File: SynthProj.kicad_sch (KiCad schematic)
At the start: 29 parts, among them J18 Ext In

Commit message: routing work...
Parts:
- added SW5: SW_DPDT_x2, SynthProjConnectors:MTS-203-A1-T0, symbol Switch:SW_DPDT_x2
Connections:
- net PT2399Echo/EchoOut: now also SW5.5 (B); no longer J?.T
- net PT2399Echo/Echo_ExtIn: now also SW5.2 (B); no longer J?.T
- new net: J?.T, SW5.1 (A)
- new net: J?.T, SW5.4 (A)
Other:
- moved on the sheet: J?
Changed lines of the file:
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@@
     (stroke (width 0) (type default))
   )
-  (wire (pts (xy 305.435 88.265) (xy 311.785 88.265))
+  (wire (pts (xy 292.735 88.265) (xy 299.085 88.265))
     (stroke (width 0) (type default))
   )
@@
     (stroke (width 0) (type default))
   )
+  (wire (pts (xy 368.3 73.025) (xy 380.365 73.025))
+    (stroke (width 0) (type default))
+  )
   (wire (pts (xy 118.11 64.135) (xy 134.62 64.135))
     (stroke (width 0) (type default))
@@
     (stroke (width 0) (type default))
   )
+  (wire (pts (xy 309.245 90.805) (xy 311.785 90.805))
+    (stroke (width 0) (type default))
+  )
   (wire (pts (xy 368.935 149.86) (xy 368.935 145.415))
     (stroke (width 0) (type default))
@@
     (stroke (width 0) (type default))
   )
-  (wire (pts (xy 311.785 88.265) (xy 311.785 77.47))
+  (wire (pts (xy 311.785 77.47) (xy 311.785 90.805))
     (stroke (width 0) (type default))
   )
@@
     (stroke (width 0) (type default))
   )
+  (wire (pts (xy 299.085 93.345) (xy 296.545 93.345))
+    (stroke (width 0) (type default))
+  )
   (wire (pts (xy 115.57 62.865) (xy 115.57 66.675))
     (stroke (width 0) (type default))
@@
     (stroke (width 0) (type default))
   )
+  (wire (pts (xy 285.75 101.6) (xy 296.545 101.6))
+    (stroke (width 0) (type default))
+  )
   (wire (pts (xy 127 118.745) (xy 127 74.295))
     (stroke (width 0) (type default))
   )
+  (wire (pts (xy 296.545 93.345) (xy 296.545 101.6))
+    (stroke (width 0) (type default))
+  )
   (wire (pts (xy 305.435 75.565) (xy 318.77 75.565))
     (stroke (width 0) (type default))
@@
     (stroke (width 0) (type default))
   )
-  (wire (pts (xy 354.965 75.565) (xy 361.315 75.565))
+  (wire (pts (xy 354.965 75.565) (xy 358.14 75.565))
     (stroke (width 0) (type default))
   )
@@
   )
   (wire (pts (xy 306.07 152.4) (xy 318.135 152.4))
+    (stroke (width 0) (type default))
+  )
+  (wire (pts (xy 382.905 78.105) (xy 368.3 78.105))
     (stroke (width 0) (type default))
   )
@@
     )
   )
-  (symbol (lib_id "power:GNDREF") (at 361.315 73.025 0) (unit 1)
+  (symbol (lib_id "power:GNDREF") (at 382.905 75.565 0) (unit 1)
     (in_bom yes) (on_board yes) (dnp no) (fields_autoplaced)
-    (property "Reference" "#PWR034" (at 361.315 79.375 0)
-      (effects (font (size 1.27 1.27)) hide)
-    )
-    (property "Value" "GNDREF" (at 361.315 77.1581 0)
-      (effects (font (size 1.27 1.27)))
-    )
-    (property "Footprint" "" (at 361.315 73.025 0)
-      (effects (font (size 1.27 1.27)) hide)
-    )
-    (property "Datasheet" "" (at 361.315 73.025 0)
+    (property "Reference" "#PWR034" (at 382.905 81.915 0)
+      (effects (font (size 1.27 1.27)) hide)
+    )
+    (property "Value" "GNDREF" (at 382.905 79.6981 0)
+      (effects (font (size 1.27 1.27)))
+    )
+    (property "Footprint" "" (at 382.905 75.565 0)
+      (effects (font (size 1.27 1.27)) hide)
+    )
+    (property "Datasheet" "" (at 382.905 75.565 0)
       (effects (font (size 1.27 1.27)) hide)
     )
@@
     )
   )
-  (symbol (lib_id "SynthProj-rescue:AudioJack2-Connector") (at 300.355 88.265 0) (unit 1)
-    (in_bom yes) (on_board yes) (dnp no)
-    (property "Reference" "J?" (at 301.1678 80.01 0)
-      (effects (font (size 1.27 1.27)))
-    )
-    (property "Value" "Echo_ExtIn" (at 301.1678 82.3214 0)
-      (effects (font (size 1.27 1.27)))
-    )
-    (property "Footprint" "SynthProjConnectors:PJ-301" (at 300.355 88.265 0)
-      (effects (font (size 1.27 1.27)) hide)
-    )
-    (property "Datasheet" "~" (at 300.355 88.265 0)
+  (symbol (lib_id "SynthProj-rescue:AudioJack2-Connector") (at 287.655 88.265 0) (unit 1)
+    (in_bom yes) (on_board yes) (dnp no)
+    (property "Reference" "J?" (at 288.4678 80.01 0)
+      (effects (font (size 1.27 1.27)))
+    )
+    (property "Value" "Echo_ExtIn" (at 288.4678 82.3214 0)
+      (effects (font (size 1.27 1.27)))
+    )
+    (property "Footprint" "SynthProjConnectors:PJ-301" (at 287.655 88.265 0)
+      (effects (font (size 1.27 1.27)) hide)
+    )
+    (property "Datasheet" "~" (at 287.655 88.265 0)
       (effects (font (size 1.27 1.27)) hide)
     )
@@
     )
   )
-  (symbol (lib_id "SynthProj-rescue:AudioJack2-Connector") (at 366.395 75.565 0) (mirror y) (unit 1)
-    (in_bom yes) (on_board yes) (dnp no)
-    (property "Reference" "J?" (at 365.5822 67.31 0)
-      (effects (font (size 1.27 1.27)))
-    )
-    (property "Value" "ECHO_OUT" (at 365.5822 69.6214 0)
-      (effects (font (size 1.27 1.27)))
-    )
-    (property "Footprint" "SynthProjConnectors:PJ-301" (at 366.395 75.565 0)
-      (effects (font (size 1.27 1.27)) hide)
-    )
-    (property "Datasheet" "~" (at 366.395 75.565 0)
+  (symbol (lib_id "SynthProj-rescue:AudioJack2-Connector") (at 387.985 78.105 0) (mirror y) (unit 1)
+    (in_bom yes) (on_board yes) (dnp no)
+    (property "Reference" "J?" (at 387.1722 69.85 0)
+      (effects (font (size 1.27 1.27)))
+    )
+    (property "Value" "ECHO_OUT" (at 387.1722 72.1614 0)
+      (effects (font (size 1.27 1.27)))
+    )
+    (property "Footprint" "SynthProjConnectors:PJ-301" (at 387.985 78.105 0)
+      (effects (font (size 1.27 1.27)) hide)
+    )
+    (property "Datasheet" "~" (at 387.985 78.105 0)
       (effects (font (size 1.27 1.27)) hide)
     )
@@
     )
   )
+  (symbol (lib_id "Switch:SW_DPDT_x2") (at 304.165 90.805 0) (mirror y) (unit 1)
+    (in_bom yes) (on_board yes) (dnp no)
+    (property "Reference" "SW5" (at 304.165 86.995 0)
+      (effects (font (size 1.27 1.27)))
+    )
+    (property "Value" "SW_DPDT_x2" (at 304.165 84.5708 0)
+      (effects (font (size 1.27 1.27)))
+    )
+    (property "Footprint" "SynthProjConnectors:MTS-203-A1-T0" (at 304.165 90.805 0)
+      (effects (font (size 1.27 1.27)) hide)
+    )
+    (property "Datasheet" "~" (at 304.165 90.805 0)
+      (effects (font (size 1.27 1.27)) hide)
+    )
+    (pin "2")
+    (pin "5")
+    (pin "3")
+    (pin "6")
+    (pin "4")
+    (pin "1")
+    (instances
+      (project "SynthProj"
+        (path "/9021c97e-351f-4ed9-b393-50257df6a463/0e948a88-c071-4754-aa3e-af223f738530"
+          (reference "SW5") (unit 1)
+        )
+        (path "/9021c97e-351f-4ed9-b393-50257df6a463"
+          (reference "SW5") (unit 1)
+        )
+      )
+    )
+  )
   (symbol (lib_id "power:GNDREF") (at 153.67 139.7 0) (unit 1)
     (in_bom yes) (on_board yes) (dnp no) (fields_autoplaced)
@@
     )
   )
+  (symbol (lib_id "Switch:SW_DPDT_x2") (at 363.22 75.565 0) (mirror x) (unit 2)
+    (in_bom yes) (on_board yes) (dnp no)
+    (property "Reference" "SW5" (at 363.22 68.4997 0)
+      (effects (font (size 1.27 1.27)))
+    )
+    (property "Value" "SW_DPDT_x2" (at 363.22 70.9239 0)
+      (effects (font (size 1.27 1.27)))
+    )
+    (property "Footprint" "SynthProjConnectors:MTS-203-A1-T0" (at 363.22 75.565 0)
+      (effects (font (size 1.27 1.27)) hide)
+    )
+    (property "Datasheet" "~" (at 363.22 75.565 0)
+      (effects (font (size 1.27 1.27)) hide)
+    )
+    (pin "2")
+    (pin "5")
+    (pin "3")
+    (pin "6")
+    (pin "4")
+    (pin "1")
+    (instances
+      (project "SynthProj"
+        (path "/9021c97e-351f-4ed9-b393-50257df6a463/0e948a88-c071-4754-aa3e-af223f738530"
+          (reference "SW5") (unit 2)
+        )
+        (path "/9021c97e-351f-4ed9-b393-50257df6a463"
+          (reference "SW5") (unit 2)
+        )
+      )
+    )
+  )
   (symbol (lib_id "SynthProj-rescue:AudioJack2-Connector") (at 64.77 34.925 0) (unit 1)
     (in_bom yes) (on_board yes) (dnp no)
@@
     )
   )
-  (symbol (lib_id "power:GNDREF") (at 305.435 85.725 0) (unit 1)
+  (symbol (lib_id "power:GNDREF") (at 292.735 85.725 0) (unit 1)
     (in_bom yes) (on_board yes) (dnp no) (fields_autoplaced)
-    (property "Reference" "#PWR033" (at 305.435 92.075 0)
-      (effects (font (size 1.27 1.27)) hide)
-    )
-    (property "Value" "GNDREF" (at 305.435 89.8581 0)
-      (effects (font (size 1.27 1.27)))
-    )
-    (property "Footprint" "" (at 305.435 85.725 0)
-      (effects (font (size 1.27 1.27)) hide)
-    )
-    (property "Datasheet" "" (at 305.435 85.725 0)
-      (effects (font (size 1.27 1.27)) hide)
-    )
+    (property "Reference" "#PWR033" (at 292.735 92.075 0)
+      (effects (font (size 1.27 1.27)) hide)
+    )
+    (property "Value" "GNDREF" (at 292.735 89.8581 0)
+      (effects (font (size 1.27 1.27)))
+    )
+    (property "Footprint" "" (at 292.735 85.725 0)
+      (effects (font (size 1.27 1.27)) hide)
+    )
+    (property "Datasheet" "" (at 292.735 85.725 0)
+      (effects (font (size 1.27 1.27)) hide)
+    )

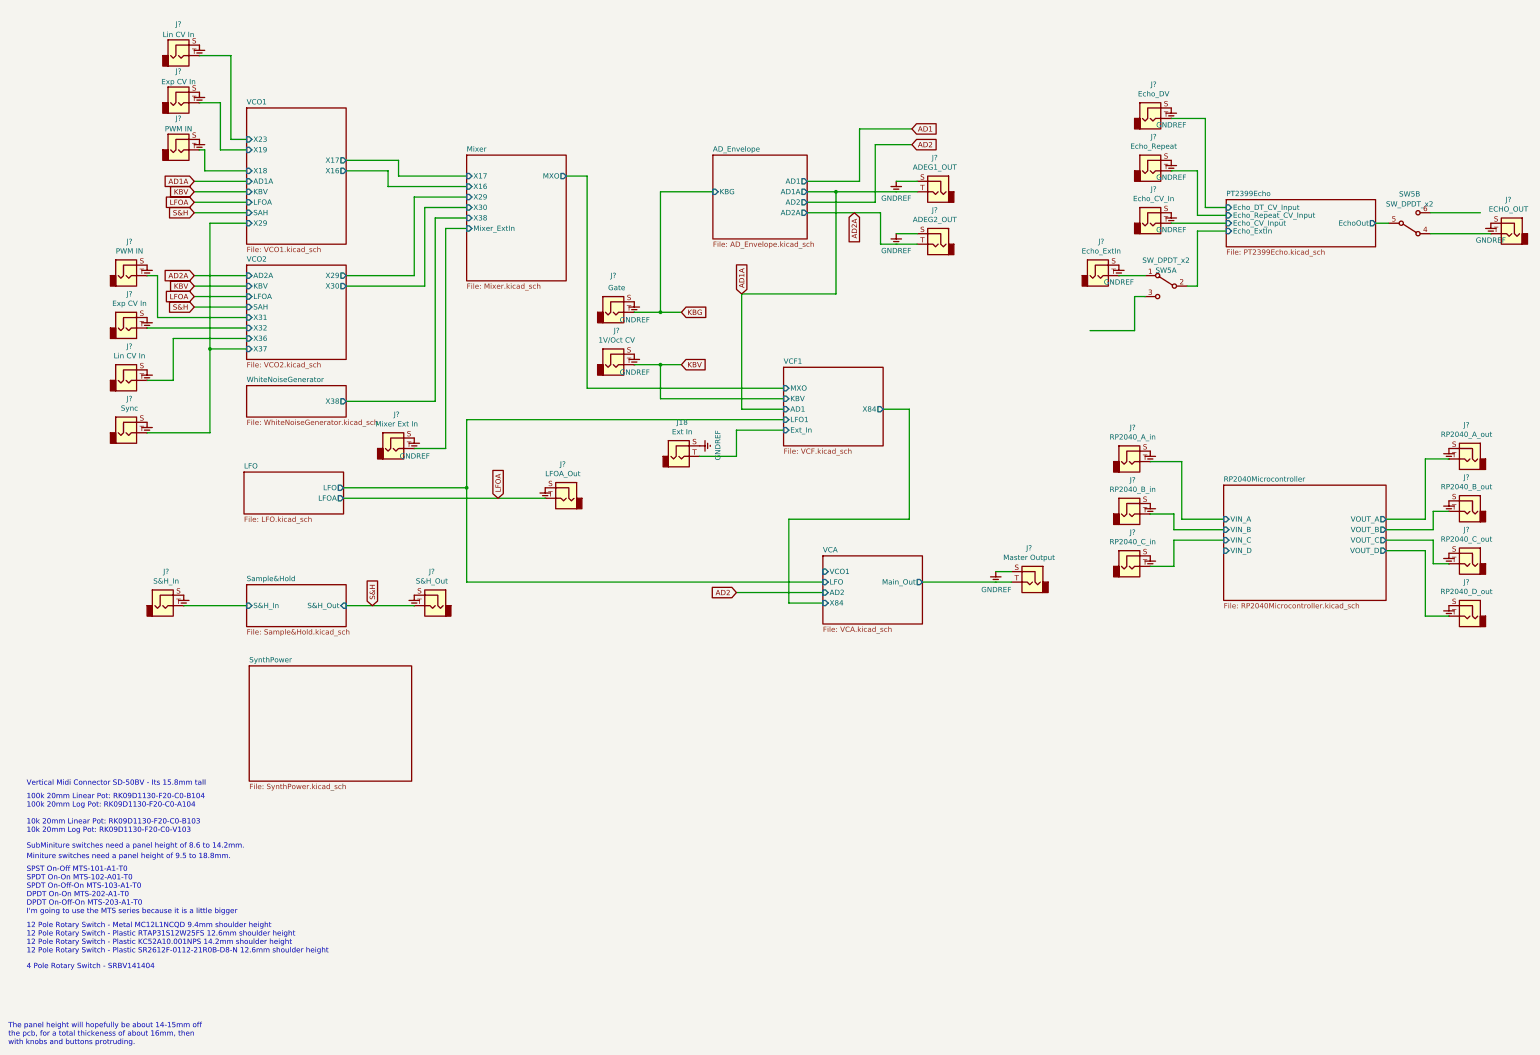
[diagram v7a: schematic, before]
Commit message: lots of routes, added vco3, lfo2.
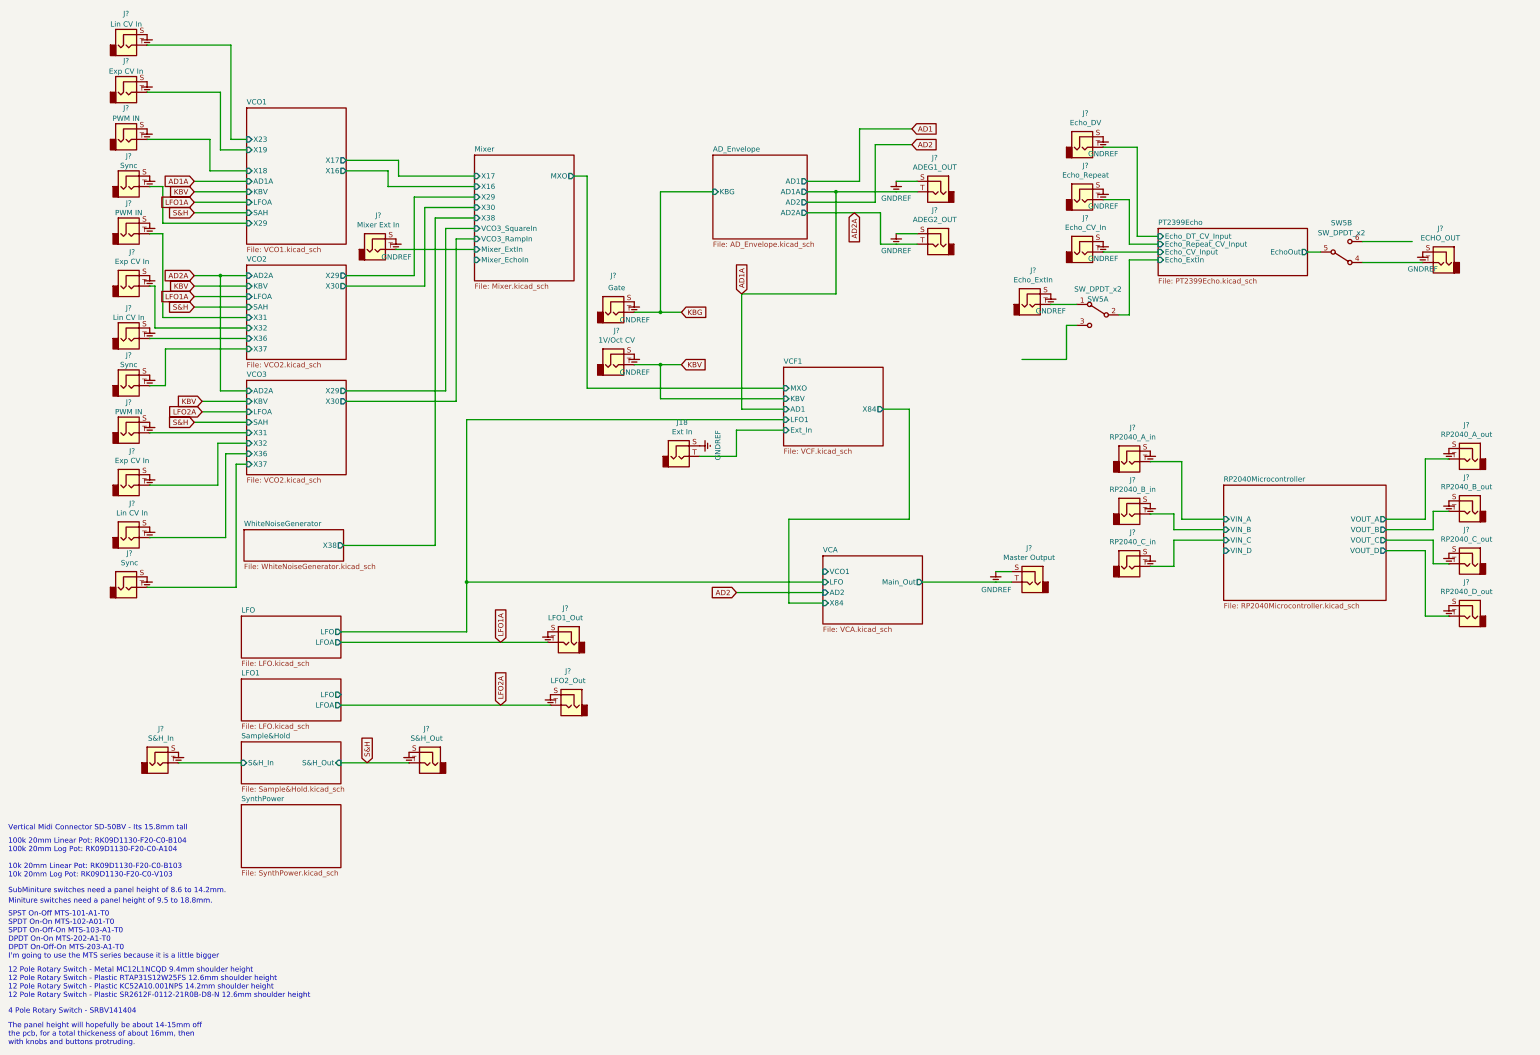
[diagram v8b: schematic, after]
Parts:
- added J?: PWM IN, SynthProjConnectors:PJ-301-BM, symbol SynthProj-rescue:AudioJack2-Connector
- added J?: Lin CV In, SynthProjConnectors:PJ-301-BM, symbol SynthProj-rescue:AudioJack2-Connector
- added J?: LFO2_Out, SynthProjConnectors:PJ-301-BM, symbol SynthProj-rescue:AudioJack2-Connector
- added J? (x2): Sync, SynthProjConnectors:PJ-301-BM, symbol SynthProj-rescue:AudioJack2-Connector
- added J?: Exp CV In, SynthProjConnectors:PJ-301-BM, symbol SynthProj-rescue:AudioJack2-Connector
- J18, J? (x27): footprint SynthProjConnectors:PJ-301 -> SynthProjConnectors:PJ-301-BM
- J?: value LFOA_Out -> LFO1_Out; footprint SynthProjConnectors:PJ-301 -> SynthProjConnectors:PJ-301-BM
- SW5: footprint SynthProjConnectors:MTS-203-A1-T0 -> SynthProjConnectors:SMTS-202
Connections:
- net GNDREF: now also J?.S, J?.S, J?.S, J?.S, J?.S, J?.S
- net VCO1/X29: now also J?.T; no longer J?.T
- net LFOA renamed LFO1A
- new net LFO2A: J?.T
- new net VCO2/X37: J?.T
- new net VCO3/X31: J?.T
- new net VCO3/X32: J?.T
- new net VCO3/X36: J?.T
- new net VCO3/X37: J?.T
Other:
- added sheet LFO1 (LFO.kicad_sch)
- added sheet VCO3 (VCO2.kicad_sch)
- sheet Mixer ports: added Mixer_EchoIn, VCO3_RampIn, VCO3_SquareIn; removed none
- moved on the sheet: J?, SW5A, SW5B
